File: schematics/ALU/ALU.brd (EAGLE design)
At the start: 65.4 x 84.1 mm, 31 parts, among them IC1 74AC08N, IC10 74AC32N, IC11 74AC32N, IC2 74AC86N, IC22 74AC86N, IC24 74AC08N, IC27 74ACT02N, IC3 74AC08N, IC36 74HC86N, IC4 74AC86N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

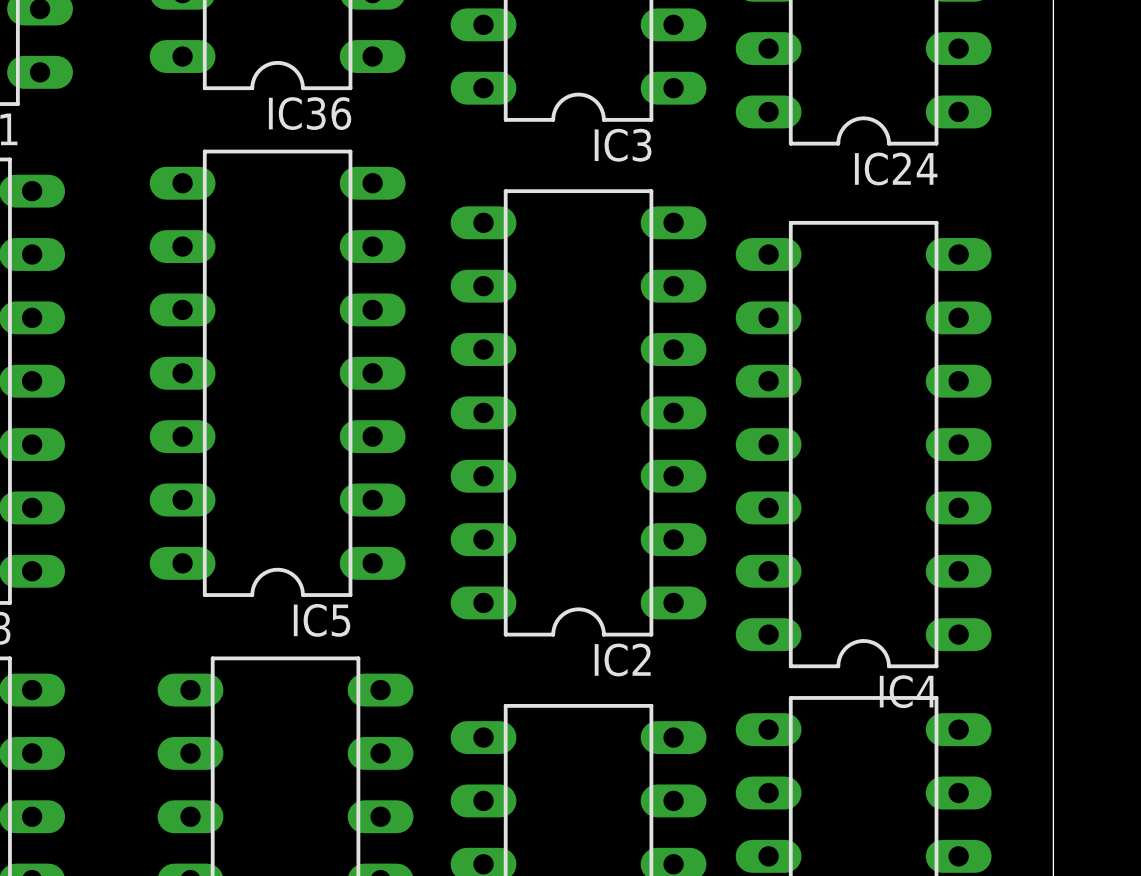
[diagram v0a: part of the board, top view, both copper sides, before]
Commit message: remove leds. I will make a interface board with them
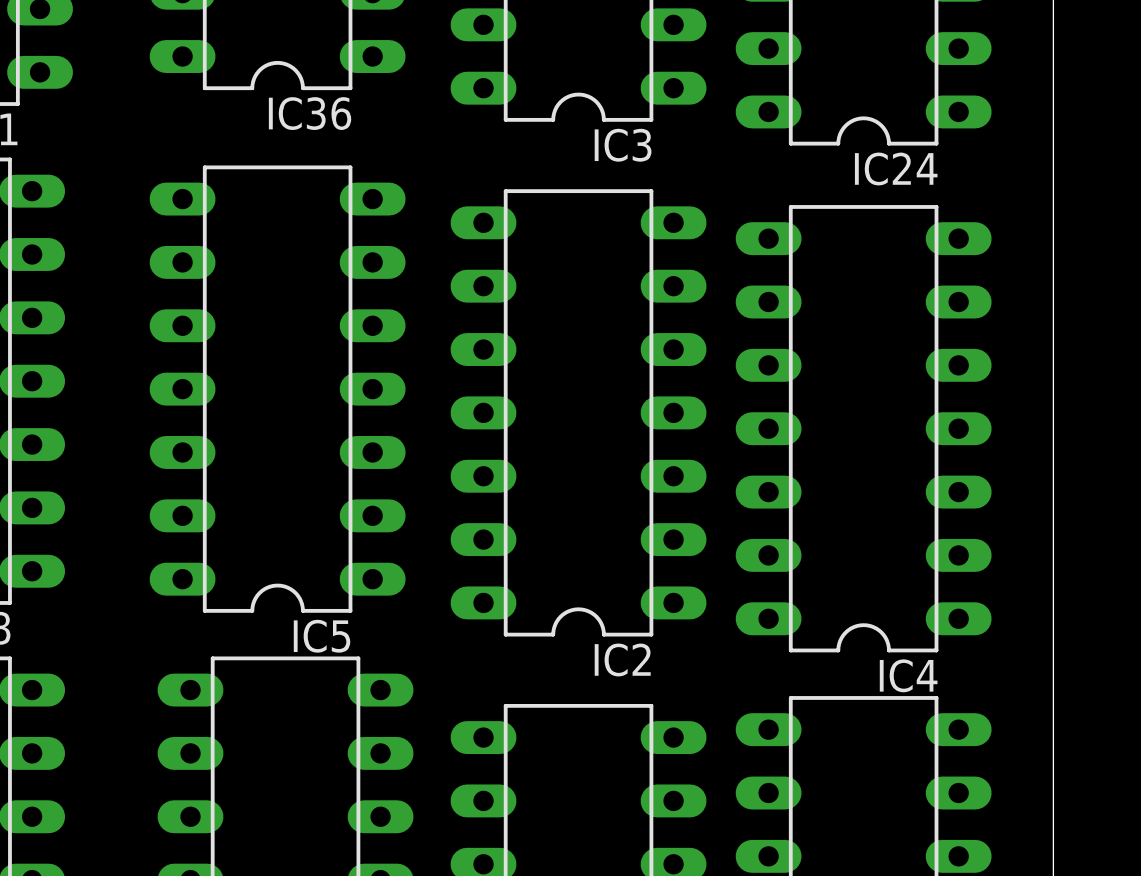
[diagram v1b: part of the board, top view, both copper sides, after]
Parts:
- moved IC5 0.64 mm to (70.5, 47.3)
- moved IC4 0.63 mm to (94.0, 45.7)
